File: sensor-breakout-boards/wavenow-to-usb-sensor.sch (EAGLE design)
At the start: 4 parts, among them X1 Type-A Receptacle, X2 Micro Type-B Receptacle

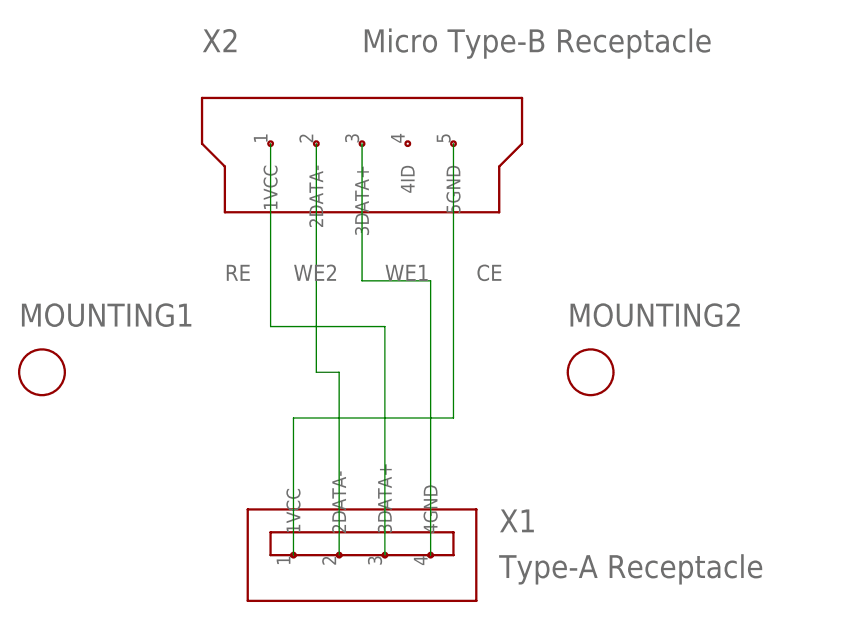
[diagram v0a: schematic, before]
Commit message: corrected wavenow-to-usb connections
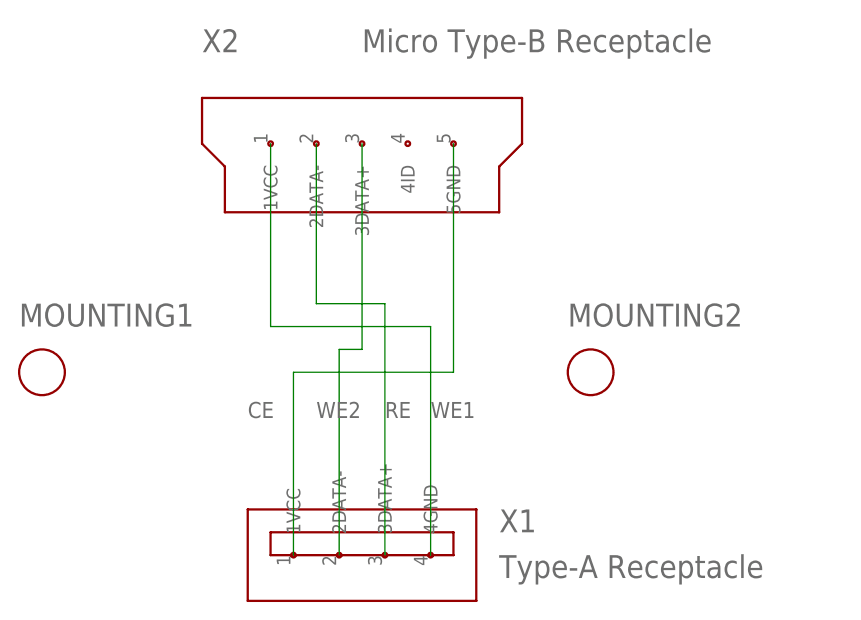
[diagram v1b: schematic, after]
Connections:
- net RE: now also X2.2DATA-; no longer X2.1VCC
- net WE1: now also X2.1VCC; no longer X2.3DATA+
- net WE2: now also X2.3DATA+; no longer X2.2DATA-
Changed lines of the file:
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@@
 </busses>
 <nets>
-<net name="RE" class="0">
+<net name="WE1" class="0">
 <segment>
 <pinref part="X2" gate="G$1" pin="1VCC"/>
 <wire x1="40.64" y1="60.96" x2="40.64" y2="40.64" width="0.1524" layer="91"/>
+<pinref part="X1" gate="G$1" pin="4GND"/>
+<wire x1="40.64" y1="40.64" x2="58.42" y2="40.64" width="0.1524" layer="91"/>
+<wire x1="58.42" y1="40.64" x2="58.42" y2="15.24" width="0.1524" layer="91"/>
+<label x="58.42" y="30.48" size="1.778" layer="95"/>
+</segment>
+</net>
+<net name="RE" class="0">
+<segment>
+<pinref part="X2" gate="G$1" pin="2DATA-"/>
+<wire x1="45.72" y1="60.96" x2="45.72" y2="43.18" width="0.1524" layer="91"/>
 <pinref part="X1" gate="G$1" pin="3DATA+"/>
-<wire x1="40.64" y1="40.64" x2="53.34" y2="40.64" width="0.1524" layer="91"/>
-<wire x1="53.34" y1="40.64" x2="53.34" y2="15.24" width="0.1524" layer="91"/>
-<label x="35.56" y="45.72" size="1.778" layer="95"/>
+<wire x1="45.72" y1="43.18" x2="53.34" y2="43.18" width="0.1524" layer="91"/>
+<wire x1="53.34" y1="43.18" x2="53.34" y2="15.24" width="0.1524" layer="91"/>
+<label x="53.34" y="30.48" size="1.778" layer="95"/>
 </segment>
 </net>
 <net name="WE2" class="0">
 <segment>
-<pinref part="X2" gate="G$1" pin="2DATA-"/>
-<wire x1="45.72" y1="60.96" x2="45.72" y2="35.56" width="0.1524" layer="91"/>
+<pinref part="X2" gate="G$1" pin="3DATA+"/>
+<wire x1="50.8" y1="60.96" x2="50.8" y2="38.1" width="0.1524" layer="91"/>
 <pinref part="X1" gate="G$1" pin="2DATA-"/>
-<wire x1="45.72" y1="35.56" x2="48.26" y2="35.56" width="0.1524" layer="91"/>
-<wire x1="48.26" y1="35.56" x2="48.26" y2="15.24" width="0.1524" layer="91"/>
-<label x="43.18" y="45.72" size="1.778" layer="95"/>
-</segment>
-</net>
-<net name="WE1" class="0">
-<segment>
-<pinref part="X2" gate="G$1" pin="3DATA+"/>
-<wire x1="50.8" y1="60.96" x2="50.8" y2="45.72" width="0.1524" layer="91"/>
-<pinref part="X1" gate="G$1" pin="4GND"/>
-<wire x1="50.8" y1="45.72" x2="58.42" y2="45.72" width="0.1524" layer="91"/>
-<wire x1="58.42" y1="45.72" x2="58.42" y2="15.24" width="0.1524" layer="91"/>
-<label x="53.34" y="45.72" size="1.778" layer="95"/>
+<wire x1="50.8" y1="38.1" x2="48.26" y2="38.1" width="0.1524" layer="91"/>
+<wire x1="48.26" y1="38.1" x2="48.26" y2="15.24" width="0.1524" layer="91"/>
+<label x="45.72" y="30.48" size="1.778" layer="95"/>
 </segment>
 </net>
@@
 <segment>
 <pinref part="X2" gate="G$1" pin="5GND"/>
-<wire x1="60.96" y1="60.96" x2="60.96" y2="30.48" width="0.1524" layer="91"/>
+<wire x1="60.96" y1="60.96" x2="60.96" y2="35.56" width="0.1524" layer="91"/>
 <pinref part="X1" gate="G$1" pin="1VCC"/>
-<wire x1="60.96" y1="30.48" x2="43.18" y2="30.48" width="0.1524" layer="91"/>
-<wire x1="43.18" y1="30.48" x2="43.18" y2="15.24" width="0.1524" layer="91"/>
-<label x="63.5" y="45.72" size="1.778" layer="95"/>
+<wire x1="60.96" y1="35.56" x2="43.18" y2="35.56" width="0.1524" layer="91"/>
+<wire x1="43.18" y1="35.56" x2="43.18" y2="15.24" width="0.1524" layer="91"/>
+<label x="38.1" y="30.48" size="1.778" layer="95"/>
 </segment>
 </net>
